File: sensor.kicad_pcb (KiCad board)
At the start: 4 copper layers, 48.3 x 27.9 mm, 64 parts, among them J1 10103594-0001LF, J2 , J4 , J5 , Q1 SI7423DN-T1-E3, U1 SN74LVC1G14DBV, U2 MAX17260SETD+, U3 MCP73831-2-OT, U4 STM32WB55xx, U5 MASWSS0115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

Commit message: First full draft
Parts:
- added REF**: OSHW-Symbol_6.7x6mm_SilkScreen, Symbol:OSHW-Symbol_6.7x6mm_SilkScreen, B.Cu at (79.8, 80.2)
- added REF**: KiCad-Logo_5mm_SilkScreen, Symbol:KiCad-Logo_5mm_SilkScreen, B.Cu at (110.9, 69.9)
- moved C35 0.72 mm to (103.1, 70.4)
- moved L1 0.60 mm to (109.5, 68.7)
- moved C16 0.43 mm to (98.8, 63.0)
- moved C21 0.43 mm to (99.8, 63.0)
- moved C23 0.38 mm to (102.0, 66.8)
- moved X2 0.36 mm to (99.3, 64.6)
- moved C30 0.28 mm to (101.4, 65.3)
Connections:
- J4 pad 10: /SWO -> /SWCLK
- J4 pad 11: unconnected-(J4-Pad11) -> /SWO
- J4 pad 12: unconnected-(J4-Pad12) -> /NRST
- J4 pad 5: unconnected-(J4-Pad5) -> /PE4
- J4 pad 7: /NRST -> +3.3V
- J4 pad 8: /SWDIO -> /PA10
- J4 pad 9: /SWCLK -> /SWDIO
- J5 pad 1: /ADC -> GND
- J5 pad 10: GND -> /PB9
- J5 pad 12: GND -> +5V
- J5 pad 2: /PB9 -> /ADC
- J5 pad 3: +3.3V -> /SPI1_MOSI
- J5 pad 4: /SPI1_MOSI -> /SPI1_MISO
- J5 pad 5: /SPI1_MISO -> /SPI1_SCK
- J5 pad 6: /SPI1_SCK -> /SPI1_NSS
- J5 pad 7: /SPI1_NSS -> /LPUART1_RX
- J5 pad 8: /LPUART1_RX -> /LPUART1_TX
- J5 pad 9: /LPUART1_TX -> /PA0
- U4 pad 30: unconnected-(U4-Pad30) -> /PE4
- U4 pad 36: /~{CHRG} -> /PA10
- U4 pad 42: /ENABLE_5V -> /PA15
- U4 pad 45: /PB5 -> /ENABLE_5V
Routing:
- net +3.3V: track 17.4 -> 115.2 mm, vias 0 -> 10
- net /NRST: track 0.00 -> 33.6 mm, vias 0 -> 1
- net VBUS: track 24.7 -> 44.4 mm, vias 2 -> 3
- net /SWO: track 0.00 -> 17.3 mm, vias 0 -> 1
- net /PB9: track 0.00 -> 15.8 mm, vias 0 -> 1
- net /SWCLK: track 0.00 -> 15.6 mm, vias 0 -> 1
- net /PA0: track 0.00 -> 15.0 mm, vias 0 -> 1
- net /SWDIO: track 0.00 -> 13.6 mm, vias 0 -> 1
- net /PA10: track 0.00 -> 11.9 mm, vias 0 -> 1
- net /PB1: track 0.00 -> 9.26 mm, vias 0 -> 1
- net unconnected-(J1-Pad6): track 0.00 -> 9.14 mm
- net /PE4: track 0.00 -> 8.92 mm, vias 0 -> 1
- net /LPUART1_RX: track 18.3 -> 10.9 mm
- net /ADC: track 18.0 -> 14.0 mm
- net /LPUART1_TX: track 16.7 -> 12.9 mm
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- added copper zone on F.Cu, net +3.3V
- added copper zone on In2.Cu, net +3.3V
- added copper zone on F.Cu, net VBUS
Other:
- outline, holes or cut-outs redrawn
- board text added: "+3.3V"
- board text added: "+5V"
- board text added: "GND"
- board text added: "PA0"
- board text added: "PA1"
- board text added: "PA10"
- board text added: "PA13/SWDIO"
- board text added: "PA14/SWCLK"
- board text added: "PA2"
- board text added: "PA3"
- board text added: "PA4"
- board text added: "PA5"
- board text added: "PA6"
- board text added: "PA7"
- board text added: "PA8"
- board text added: "PB1"
- board text added: "PB3/SWO"
- board text added: "PE4"
- board text added: "RST"

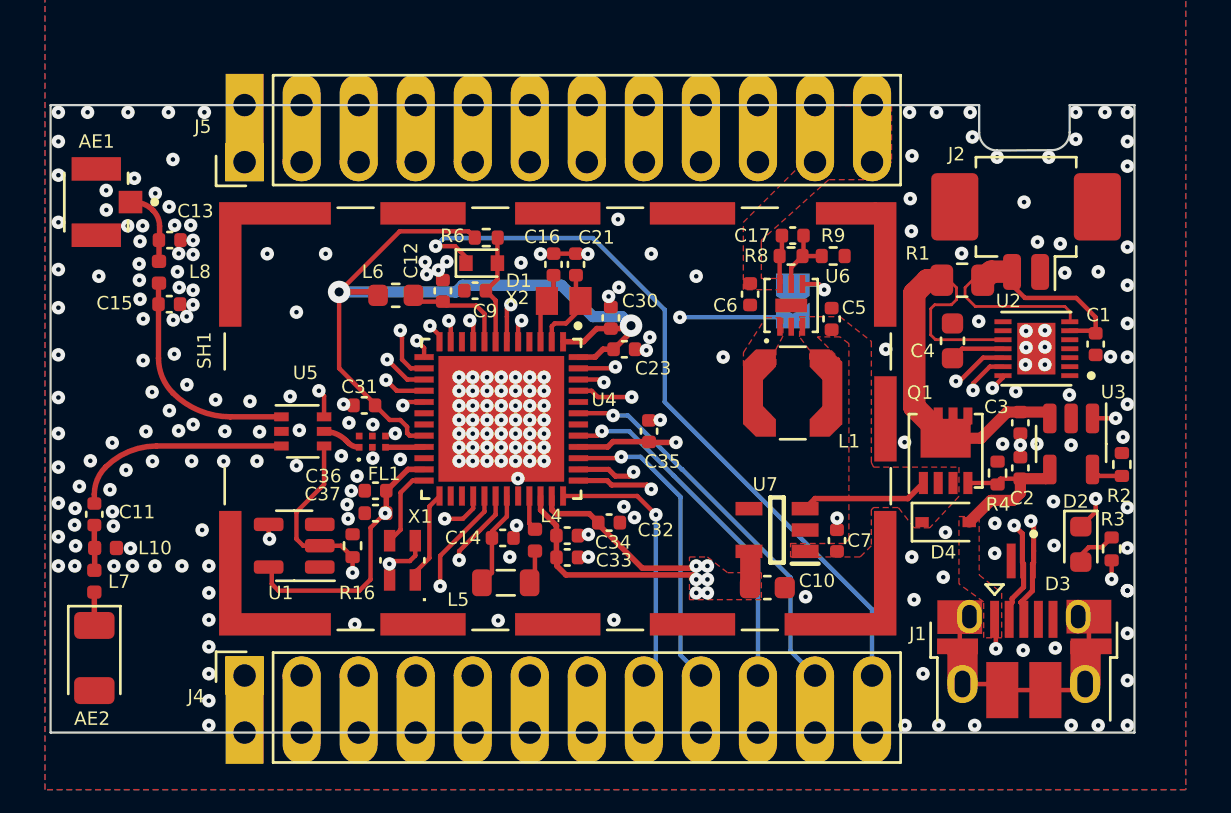
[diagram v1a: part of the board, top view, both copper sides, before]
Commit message: Added I2C ports, rev2
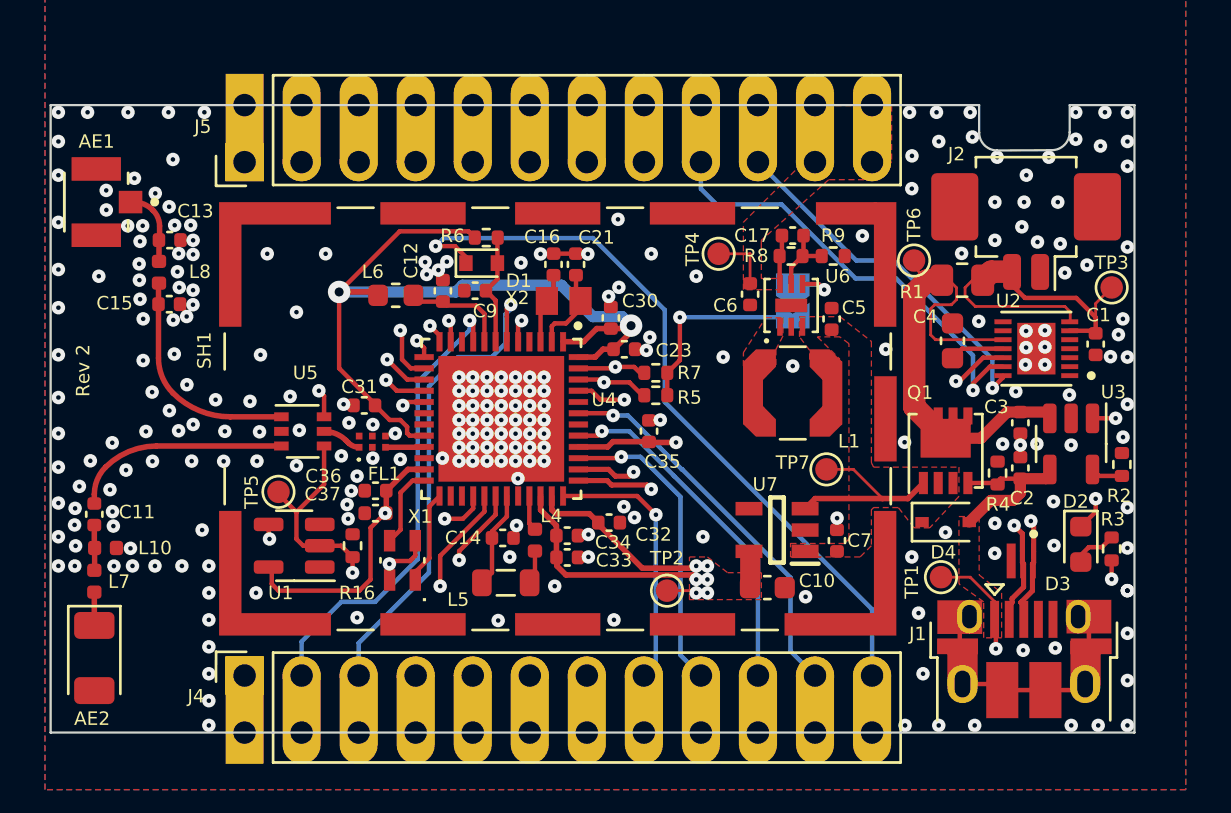
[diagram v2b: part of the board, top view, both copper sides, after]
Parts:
- added R5: 1k, Resistor_SMD:R_0402_1005Metric, F.Cu at (103.4, 68.8)
- added R7: 1k, Resistor_SMD:R_0402_1005Metric, F.Cu at (103.4, 67.8)
- added TP1: TestPoint, TestPoint:TestPoint_Pad_D1.0mm, F.Cu at (116.1, 76.9)
- added TP2: TestPoint, TestPoint:TestPoint_Pad_D1.0mm, F.Cu at (103.9, 77.5)
- added TP3: TestPoint, TestPoint:TestPoint_Pad_D1.0mm, F.Cu at (123.7, 64.0)
- added TP4: TestPoint, TestPoint:TestPoint_Pad_D1.0mm, F.Cu at (106.2, 62.5)
- added TP5: TestPoint, TestPoint:TestPoint_Pad_D1.0mm, F.Cu at (86.6, 73.1)
- added TP6: TestPoint, TestPoint:TestPoint_Pad_D1.0mm, F.Cu at (114.9, 62.8)
- added TP7: TestPoint, TestPoint:TestPoint_Pad_D1.0mm, F.Cu at (111.0, 72.1)
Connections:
- J4 pad 2: /PB8 -> /PA0
- J4 pad 3: /PB0 -> /PB9
- J5 pad 10: /PB9 -> /I2C_SCL
- J5 pad 9: /PA0 -> /I2C_SDA
- U4 pad 44: /~{FAULT} -> unconnected-(U4-Pad44)
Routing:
- net /I2C_SDA: track 25.6 -> 45.7 mm
- net /I2C_SCL: track 25.7 -> 43.8 mm
- net /PB9: track 15.8 -> 22.5 mm
- net /PA0: track 15.0 -> 20.8 mm
- net +3.3V: track 115.2 -> 120.3 mm
- net VBUS: track 44.4 -> 48.0 mm
- net VDD: track 5.74 -> 8.78 mm
- net +5V: track 2.04 -> 4.76 mm
- net /BAT_SENSE: track 14.1 -> 15.7 mm
- net /ANT_SEL: track 15.3 -> 16.5 mm
- net +BATT: track 20.5 -> 21.6 mm
- net GND: vias 243 -> 255
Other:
- board text added: "PB6"
- board text added: "PB7"
- board text added: "Rev 2"
